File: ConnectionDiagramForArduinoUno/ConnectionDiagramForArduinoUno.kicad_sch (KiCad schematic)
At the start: 18 parts, among them M1 Stepper_Motor_bipolar, SW1 SW_Push, SW2 SW_Push, SW3 SW_Push, SW4 SW_Push, SW5 SW_Push, SW6 SW_Push, SW7 SW_Push

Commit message: Kicad schematic updated.
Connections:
- net at A1.4 (3V3): now also DRV1.1 (PUL+), DRV1.3 (DIR+), DRV1.5 (ENA+), DRV1.6 (ENA-)
- now unconnected: A1.6 (GND)
- no-connect marks 14 -> 13

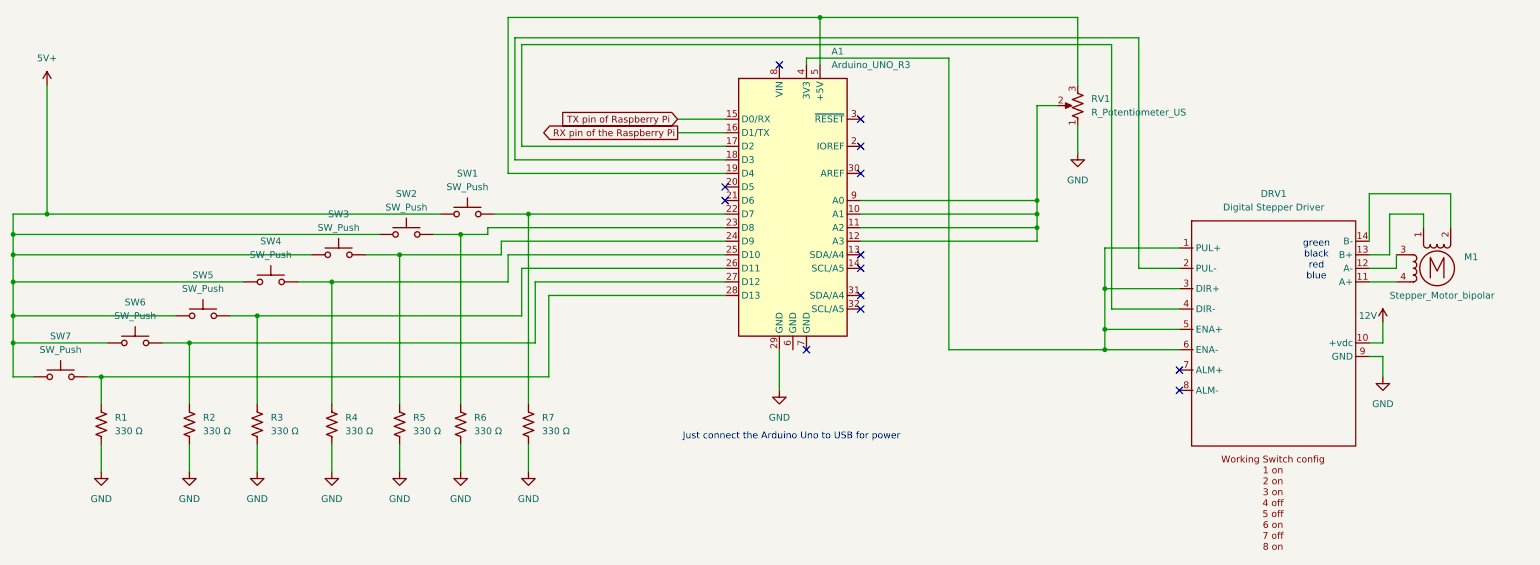
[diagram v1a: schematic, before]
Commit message: Simplified connections added for Arduino Uno to the Hardware.
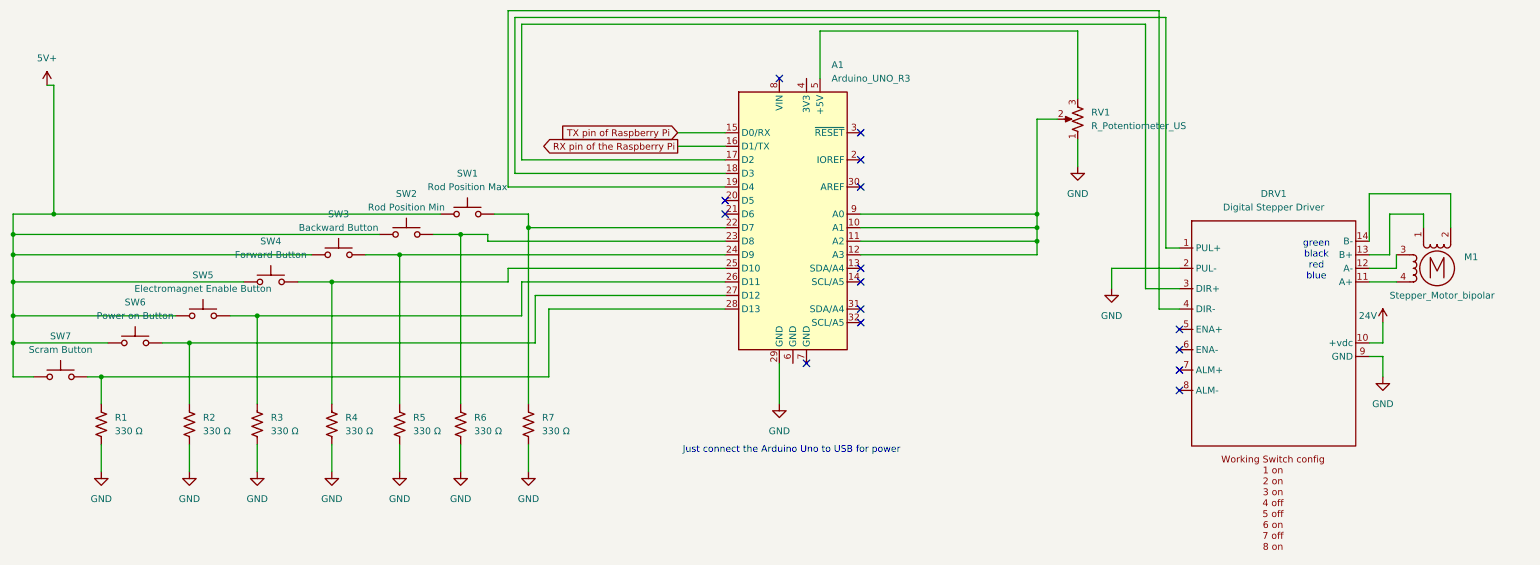
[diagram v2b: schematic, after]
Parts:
- SW1: value SW_Push -> Rod Position Max
- SW2: value SW_Push -> Rod Position Min
- SW3: value SW_Push -> Backward Button
- SW4: value SW_Push -> Forward Button
- SW5: value SW_Push -> Electromagnet Enable Button
- SW6: value SW_Push -> Power on Button
- SW7: value SW_Push -> Scram Button
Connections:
- net GND: now also DRV1.2 (PUL-)
- net at A1.5 (+5V), RV1.3: no longer A1.19 (D4)
- net at A1.17 (D2): now also DRV1.3 (DIR+); no longer DRV1.4 (DIR-)
- net at A1.18 (D3): now also DRV1.1 (PUL+); no longer DRV1.2 (PUL-)
- net 12V renamed 24V
- new net: A1.19 (D4), DRV1.4 (DIR-)
- now unconnected: A1.4 (3V3), DRV1.5 (ENA+), DRV1.6 (ENA-)
- no-connect marks 13 -> 15
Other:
- moved on the sheet: A1, RV1
